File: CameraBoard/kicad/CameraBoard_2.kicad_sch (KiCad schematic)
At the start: 40 parts, among them Q2 BVSS123LT1G, Q3 BSS84, U4 TS5A3159ADBVR, U5 ICM7242IBAZ-SMD, U6 H11F1SR2M, U7 H11F1SR2M, U8 SN74LVC1G17DCKR

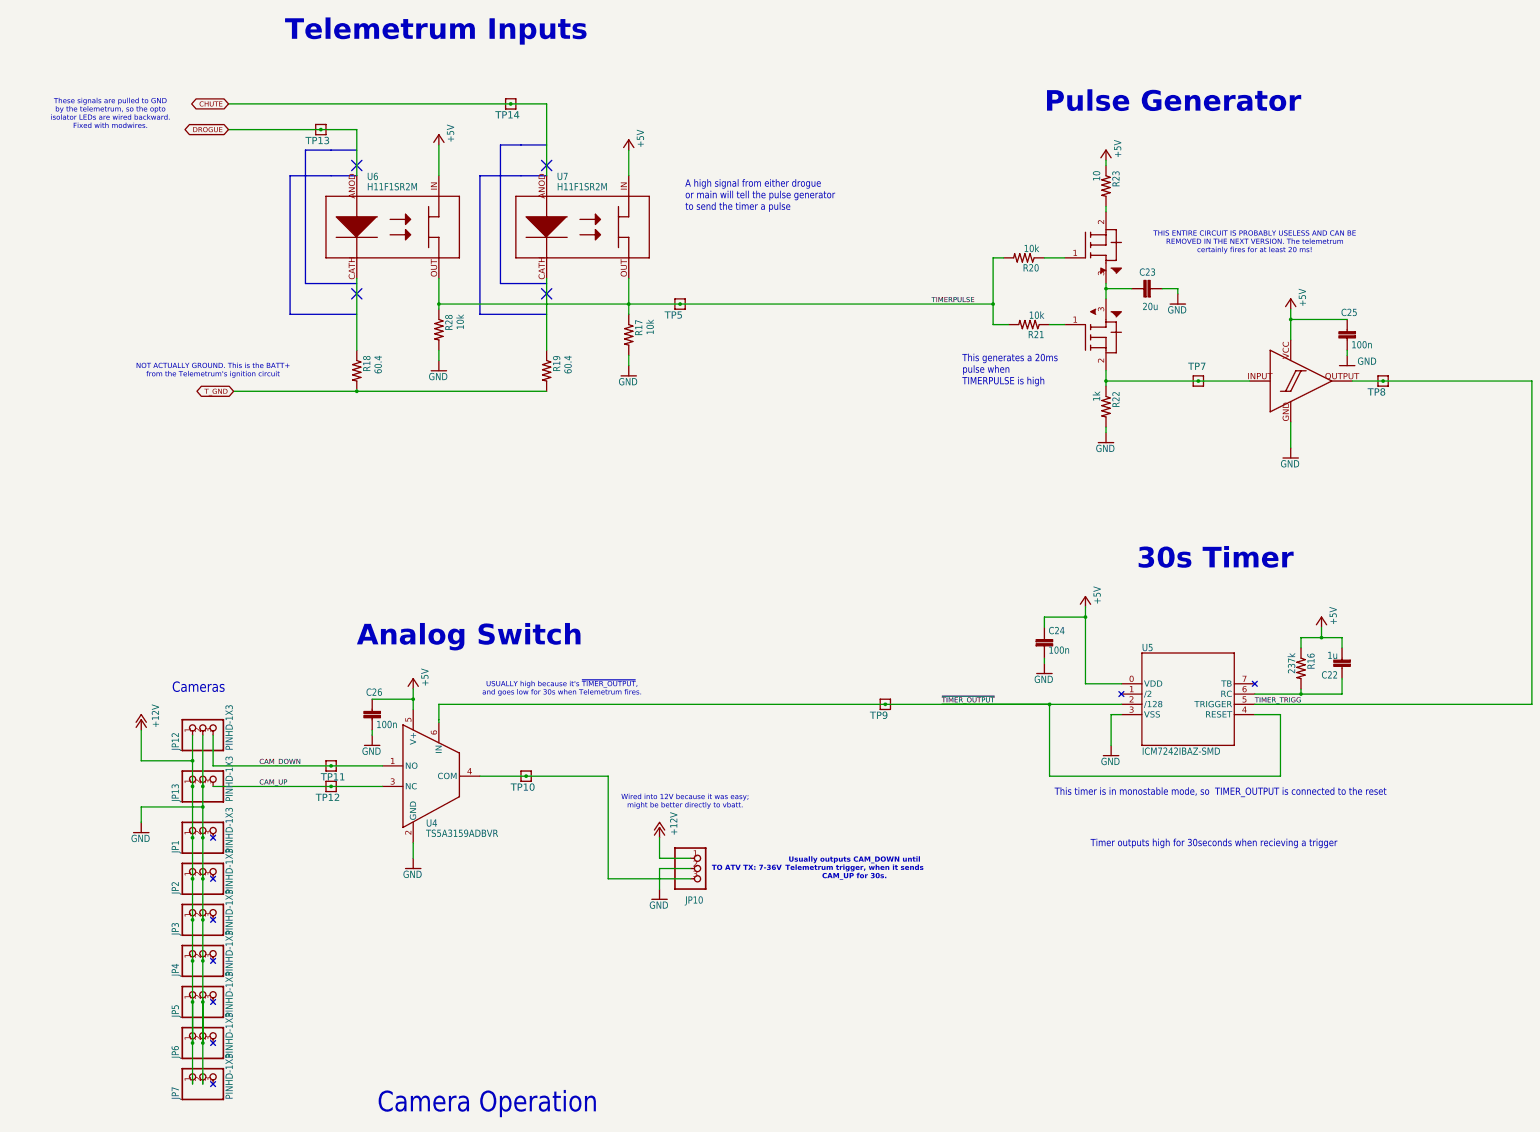
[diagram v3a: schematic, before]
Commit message: replaced the timer logic for a d flip flop
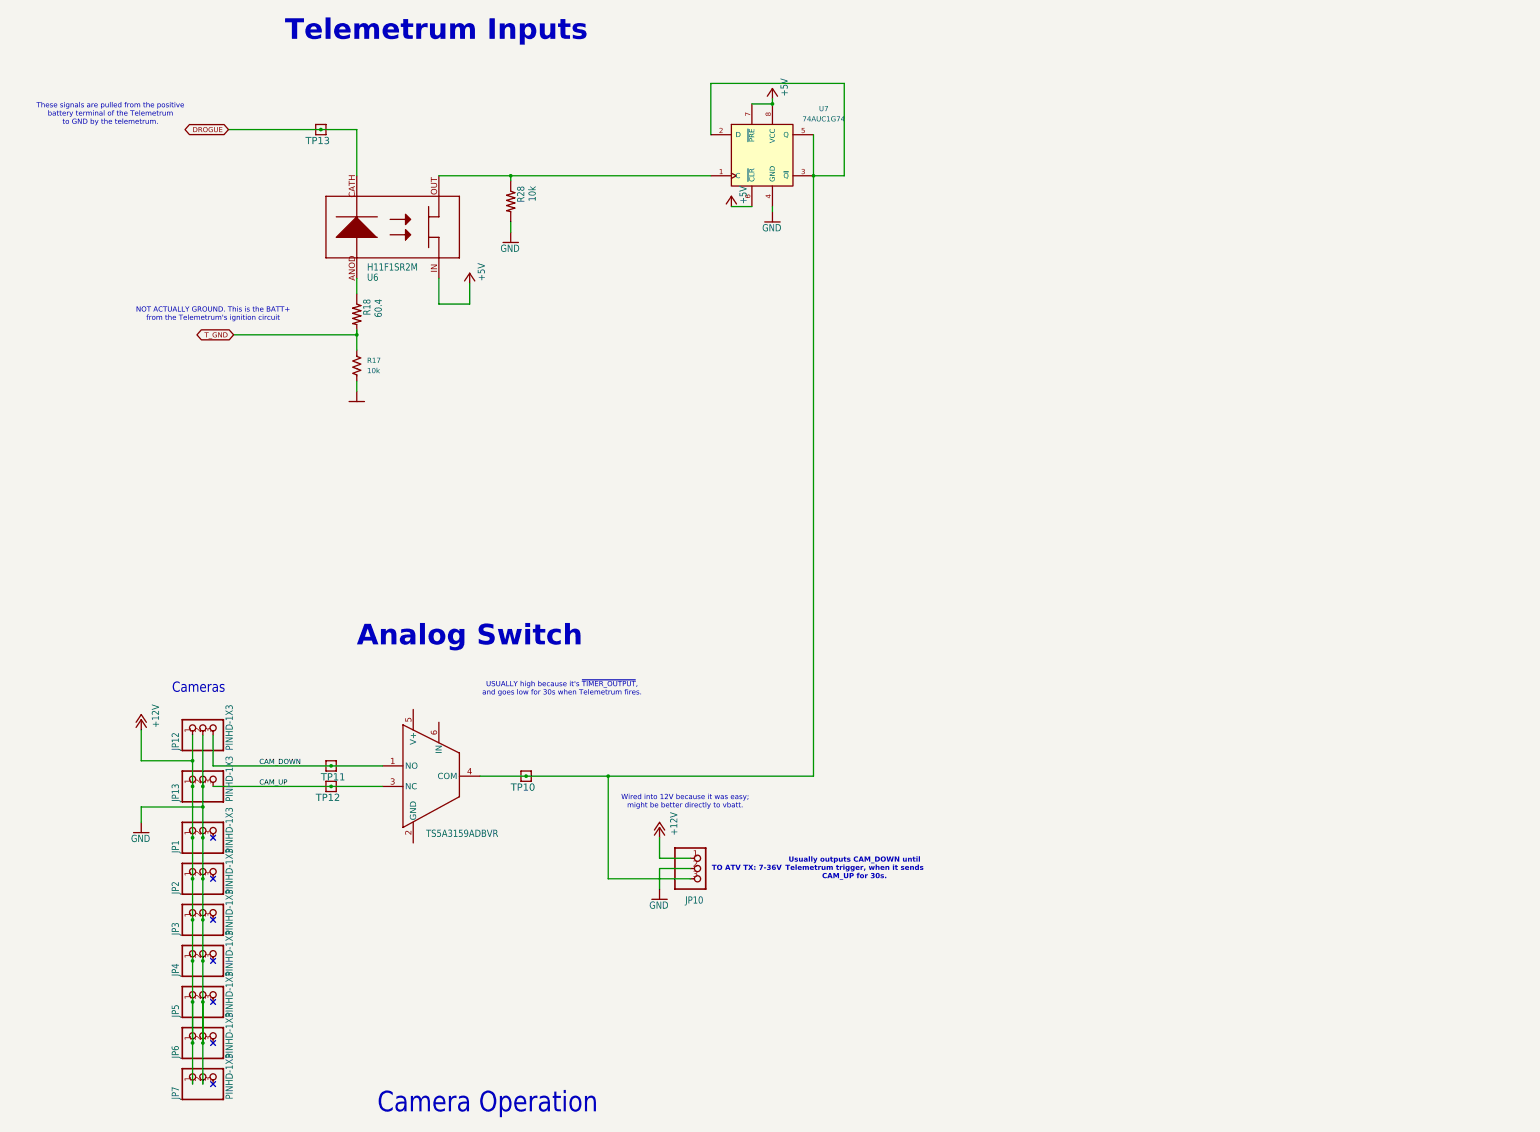
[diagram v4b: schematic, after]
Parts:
- removed C22: 1u, CameraBoard:.0603-C-NOSILK, symbol CameraBoard-eagle-import:C-EU0603-C-NOSILK
- removed C23: 20u, CameraBoard:.0603-C-NOSILK, symbol CameraBoard-eagle-import:C-EU0603-C-NOSILK
- removed C24, C25, C26: 100n, CameraBoard:.0603-C-NOSILK, symbol CameraBoard-eagle-import:C-EU0603-C-NOSILK
- removed Q2: BVSS123LT1G, CameraBoard:BVSS123LT1G, symbol CameraBoard-eagle-import:BVSS123LT1G
- removed Q3: BSS84, CameraBoard:BSS84, symbol CameraBoard-eagle-import:BSS84
- removed R16: 237k, CameraBoard:.0603-A-NOSILK, symbol CameraBoard-eagle-import:R-US_0603-A-NOSILK
- removed R17: 10k, CameraBoard:.0603-C-NOSILK, symbol CameraBoard-eagle-import:R-US_0603-C-NOSILK
- removed R19: 60.4, CameraBoard:.0603-C-NOSILK, symbol CameraBoard-eagle-import:R-US_0603-C-NOSILK
- removed R20, R21: 10k, CameraBoard:.0603-A-NOSILK, symbol CameraBoard-eagle-import:R-US_0603-A-NOSILK
- removed R22: 1k, CameraBoard:.0603-A-NOSILK, symbol CameraBoard-eagle-import:R-US_0603-A-NOSILK
- removed R23: 10, CameraBoard:.0805-A-NOSILK, symbol CameraBoard-eagle-import:R-US_0805-A-NOSILK
- removed TP14, TP5, TP7, TP8, TP9: TEST-POINT, CameraBoard:2MM-TEST-POINT, symbol CameraBoard-eagle-import:TEST-POINT
- removed U5: ICM7242IBAZ-SMD, CameraBoard:ICM7242IBAZ-SMD, symbol CameraBoard-eagle-import:ICM7242IBAZ-SMD
- removed U7: H11F1SR2M, CameraBoard:H11F1SR2M, symbol CameraBoard-eagle-import:H11F1SR2M
- removed U8: SN74LVC1G17DCKR, CameraBoard:SN74LVC1G17DCKR, symbol CameraBoard-eagle-import:SN74LVC1G17DCKR
- added R17: 10k, symbol Device:R_US
- added U7: 74AUC1G74, Package_DIP:DIP-8_W7.62mm, symbol 74xGxx:74AUC1G74
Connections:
- net +5V: now also U7.6 (~{CLR}), U7.7 (~{PRE}), U7.8 (VCC); no longer U4.5 (V+)
- net DROGUE: now also U6.CATH (CAT); no longer U6.ANOD
- net GND: now also U7.4 (GND); no longer U4.2 (GND)
- net T_GND: now also R17.1
- net at R18.1: now also U6.ANOD; no longer U6.CATH (CAT)
- net at JP10.3, TP10.1, U4.4 (COM): now also U7.2 (D), U7.3 (~{Q}), U7.5 (Q)
- net TIMERPULSE: no longer names the net of R28.1, U6.OUT
- net TIMERPULSE: now also U7.1 (C)
- net ~{TIMER_OUTPUT}: no longer names the net of U4.6 (IN)
- no-connect marks 9 -> 7
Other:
- note added: "These signals are pulled from the positive battery terminal of the Telemetrum to GND by the telemetrum."
- note removed: "30s Timer"
- note removed: "A high signal from either drogue or main will tell the pulse generator to send the timer a pulse"
- note removed: "Pulse Generator"
- note removed: "THIS ENTIRE CIRCUIT IS PROBABLY USELESS AND CAN BE REMOVED IN THE NEXT VERSION. The telemetrum certainly fires for at least 20 ms!"
- note removed: "These signals are pulled to GND by the telemetrum, so the opto isolator LEDs are wired backward. Fixed with modwires."
- note removed: "This generates a 20ms pulse when TIMERPULSE is high"
- note removed: "This timer is in monostable mode, so TIMER_OUTPUT is connected to the reset"
- note removed: "Timer outputs high for 30seconds when recieving a trigger"
- moved on the sheet: R18, R28
